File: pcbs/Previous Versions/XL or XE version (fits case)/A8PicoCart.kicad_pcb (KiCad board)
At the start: 2 copper layers, 53.8 x 70 mm, 6 parts, among them J7 Conn_01x20, J8 Conn_01x20, SW1 SW_Push, U2 Atari8Cartridge

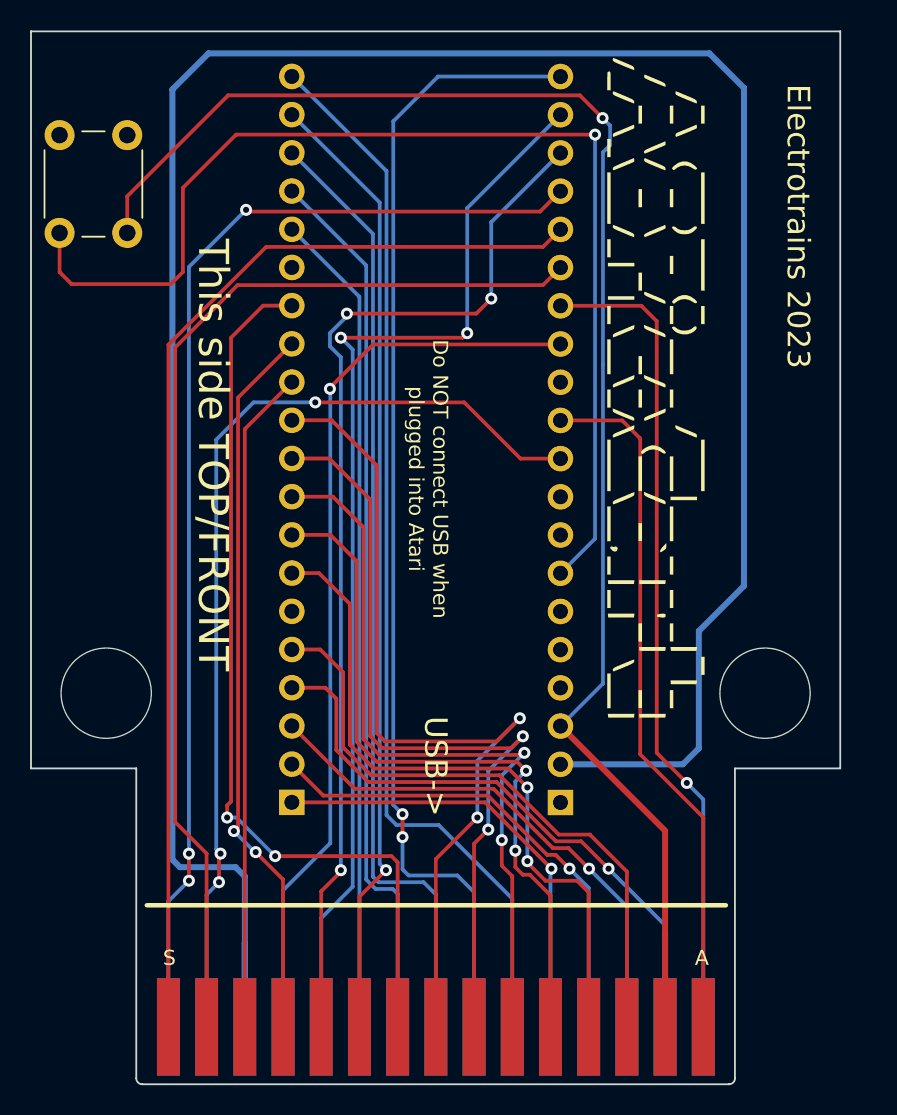
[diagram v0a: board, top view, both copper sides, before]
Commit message: update pcb, case
remove risk of back powering atari from USB by making it physically impossible on the XL/XE/cased board
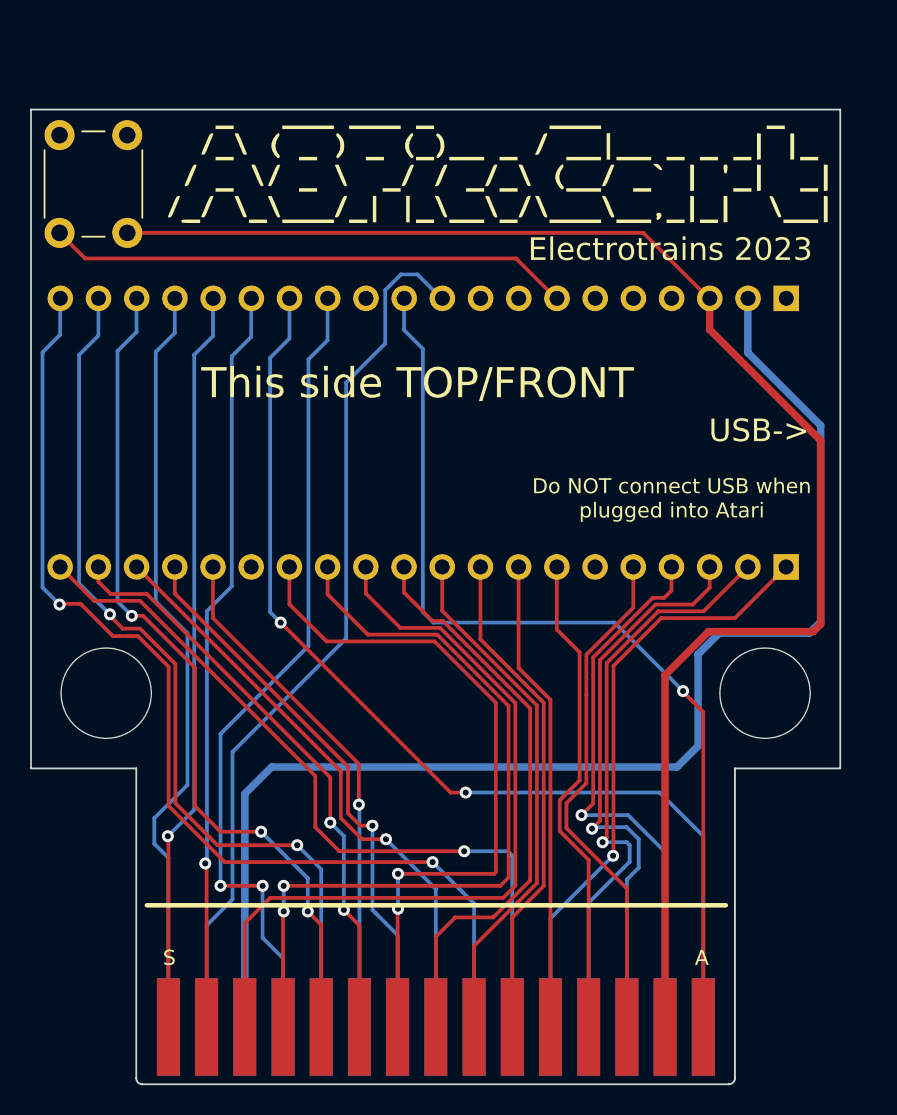
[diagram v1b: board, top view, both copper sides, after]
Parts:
- U2: footprint Atari 8-bit Cartridge:Atari8Cartridge MountHoles (taller) -> Atari 8-bit Cartridge:Atari8Cartridge MountHoles
- moved J8 36.7 mm to (179.5, 70.2), turned to 90 degrees
- moved J7 36.4 mm to (179.5, 88.0), turned to 90 degrees
- moved G*** 17.6 mm to (160.4, 62.0), turned to 0 degrees
- moved G*** 17.5 mm to (160.2, 62.1), turned to 180 degrees
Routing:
- net +5V: track 164.4 -> 83.5 mm
- net RESET: track 76.0 -> 34.9 mm, vias 1 -> 0
- net CCTL: track 78.0 -> 49.0 mm, vias 3 -> 0
- net PHI2: track 74.6 -> 47.5 mm, vias 0 -> 1
- net D3: track 64.0 -> 37.1 mm, vias 1 -> 2
- net R/W: track 73.9 -> 47.6 mm, vias 0 -> 1
- net D2: track 63.8 -> 37.7 mm, vias 0 -> 1
- net D1: track 59.2 -> 35.1 mm, vias 0 -> 1
- net D0: track 54.9 -> 32.5 mm, vias 0 -> 1
- net D4: track 70.9 -> 49.3 mm, vias 0 -> 1
- net A9: track 57.9 -> 36.4 mm, vias 2 -> 0
- net A8: track 53.5 -> 32.8 mm, vias 2 -> 0
- net A7: track 50.0 -> 31.1 mm, vias 2 -> 0
- net A6: track 47.7 -> 29.4 mm, vias 2 -> 0
- net D7: track 70.5 -> 54.4 mm
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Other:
- board size 53.8 x 70 mm -> 53.8 x 64.8 mm
- board text added: "This is the BACK/BOTTOM If you can see this... you've got it the WRONG WAY"
